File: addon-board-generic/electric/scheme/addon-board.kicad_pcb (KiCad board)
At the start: 2 copper layers, 57 parts, among them K1 CONN_3, K2 CONN_3, K3 CONN_3, K4 CONN_3, K5 CONN_3, K6 CONN_3, P1 TST, P10 CONN_6, P11 CONN_10, P12 CONN_4, P13 CONN_4, P2 TST, P3 cross board conn, P4 cross board conn, P5 TST, P6 TST, P7 TST, P8 TST, P9 CONN_4, Q1 NPN, Q2 MOS_P, Q3 BC847, Q4 BC847, Q5 MOS_P, Q6 MOS_P, U1 L293, U2 L293, U3 74HC165

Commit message: Added shift registers to increase IO pins number.
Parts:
- added K7, K8: CONN_3, PIN_ARRAY_3X1, F.Cu at (0.00, 0.00)
- added P10: CONN_8, PIN_ARRAY-8X1, F.Cu at (0.00, 0.00)
- added U4: 74HC595_MY, SO16E, F.Cu at (184.0, 157.5)
- added U5: 74HC595_MY, SO16E, F.Cu at (196.0, 157.5)
- P1, P2, P8: footprint PIN_ARRAY_1 -> m3-screw-hole
- P10: footprint PIN_ARRAY-6X1 -> PIN_ARRAY-8X1
- moved P9 285.0 mm to (185.5, 175.0)
- moved U2 276.7 mm to (212.5, 142.0)
- moved U1 259.0 mm to (194.5, 142.0)
- moved stm1 257.6 mm to (164.5, 156.5)
- moved P8 256.6 mm to (212.9, 157.0)
- moved U3 249.8 mm to (170.0, 169.5), turned to 180 degrees
- moved P2 220.6 mm to (148.0, 176.0)
- moved P3 214.8 mm to (145.5, 158.5), turned to 90 degrees
- moved P4 214.7 mm to (148.1, 158.5), turned to 90 degrees
- moved P1 190.0 mm to (148.1, 136.4)
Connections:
- P10 pad 6: GND -> /adc6
- P12 pad 1: /out4 -> /out3
- P12 pad 2: /out3 -> /out4
- P13 pad 1: /out8 -> /out7
- P13 pad 2: /out7 -> /out8
- U1 pad 13: /out4 -> /out3
- U1 pad 18: /out3 -> /out4
- U2 pad 13: /out8 -> /out7
- U2 pad 18: /out7 -> /out8
- stm1 pad 10: /adc4 -> /servo8
- stm1 pad 11: /adc5 -> /adc1
- stm1 pad 12: /servo6 -> /adc2
- stm1 pad 13: /wakeup -> /adc3
- stm1 pad 14: /servo-en -> /adc4
- stm1 pad 15: /adc1 -> /adc5
- stm1 pad 16: /adc2 -> /adc6
- stm1 pad 17: /adc3 -> /adc7
- stm1 pad 18: /addr0 -> /servo7
- stm1 pad 19: /addr1 -> /servo6
- stm1 pad 2: /moto8 -> (no net)
- stm1 pad 27: /led1 -> /addr0
- stm1 pad 28: /led2 -> /addr1
- stm1 pad 29: /moto-en1 -> /mr
- stm1 pad 3: /moto4 -> (no net)
- stm1 pad 30: /moto-en2 -> /oe
- stm1 pad 31: /moto5 -> /shcp
- stm1 pad 32: /moto6 -> /stcp
- stm1 pad 33: /moto7 -> /ds
- stm1 pad 4: /moto3 -> (no net)
- stm1 pad 5: /moto1 -> /wakeup
- stm1 pad 6: /moto2 -> (no net)
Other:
- board outline added: 85 x 56 mm
- net class Default: clearance 0.254 -> 0.2; trace_width 0.254 -> 0.25; via_dia 0.889 -> 0.9; via_drill 0.635 -> 0.6
- net class Power added: clearance 0.2, trace_width 0.5, via_dia 1, via_drill 0.7
- rule trace_clearance: 0.254 -> 0.2
- rule trace_min: 0.254 -> 0.1524
- rule via_min_drill: 0.508 -> 0.5
- rule via_min_size: 0.889 -> 0.8

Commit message: Placing components.
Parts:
- removed the P10 at (0.00, 0.00)
- moved P11 262.7 mm to (203.5, 178.2)
- moved Q6 258.0 mm to (208.8, 129.5), turned to 90 degrees
- moved R15 251.7 mm to (201.2, 134.5), turned to 180 degrees
- moved Q4 251.5 mm to (201.2, 131.8), turned to 180 degrees
- moved R17 248.9 mm to (206.8, 132.2), turned to 180 degrees
- moved R13 248.1 mm to (204.0, 133.8), turned to 270 degrees
- moved R7 245.8 mm to (184.2, 170.5), turned to 270 degrees
- moved R19 245.7 mm to (205.8, 129.5), turned to 90 degrees
- moved R8 245.6 mm to (179.2, 170.5), turned to 270 degrees
- moved R5 233.5 mm to (174.2, 162.5), turned to 270 degrees
- moved P10 232.4 mm to (163.8, 178.2)
- moved C5 232.0 mm to (178.5, 157.0), turned to 180 degrees
- moved D2 231.4 mm to (175.0, 127.2)
- moved C2 226.3 mm to (164.2, 154.0)
- moved C4 224.6 mm to (178.2, 147.2), turned to 270 degrees
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
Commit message: Placing components.
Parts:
- moved Q5 243.1 mm to (221.5, 74.5), turned to 90 degrees
- moved R16 235.9 mm to (219.5, 77.2), turned to 180 degrees
- moved Q3 235.6 mm to (215.5, 76.5), turned to 90 degrees
- moved R18 233.6 mm to (218.5, 74.5), turned to 90 degrees
- moved R14 230.7 mm to (213.8, 73.8)
- moved R12 229.9 mm to (212.8, 76.5), turned to 90 degrees
- moved R3 225.6 mm to (151.5, 170.0)
- moved C7 217.7 mm to (194.0, 74.8)
- moved Q2 217.1 mm to (194.0, 77.5), turned to 90 degrees
- moved R11 214.8 mm to (190.2, 78.2), turned to 180 degrees
- moved R10 210.6 mm to (187.2, 75.5), turned to 90 degrees
- moved R9 210.5 mm to (185.2, 75.5), turned to 90 degrees
- moved Q1 210.5 mm to (190.2, 75.5), turned to 90 degrees
- moved R15 75.7 mm to (214.5, 60.0), turned to 0 degrees
- moved U2 71.9 mm to (230.2, 63.5)
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
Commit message: Started routing.
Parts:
- added C10: 18p, SM0805, F.Cu at (152.9, 165.4)
- added C8: 10u, SM0805, F.Cu at (184.5, 135.6)
- added C9: 18p, SM0805, F.Cu at (152.9, 161.5)
- added R20: 50, SM0805, F.Cu at (159.0, 164.3)
- added X1: 8MHz, C2, F.Cu at (155.7, 163.6)
- C7: value 10u -> 100n
- P10: value CONN_6 -> CONN_8
- moved R15 104.2 mm to (220.1, 164.1), turned to 90 degrees
- moved R13 102.8 mm to (222.9, 165.1), turned to 180 degrees
- moved Q4 99.8 mm to (222.9, 162.3), turned to 180 degrees
- moved R19 98.9 mm to (220.9, 159.6), turned to 180 degrees
- moved Q6 96.1 mm to (220.9, 156.8), turned to 180 degrees
- moved R17 95.4 mm to (223.6, 158.8), turned to 270 degrees
- moved R14 95.3 mm to (206.6, 168.8), turned to 90 degrees
- moved R12 93.3 mm to (209.3, 169.8), turned to 180 degrees
- moved Q3 90.7 mm to (209.3, 167.0), turned to 180 degrees
- moved R18 90.2 mm to (207.3, 164.0), turned to 180 degrees
- moved Q5 87.7 mm to (207.3, 161.0), turned to 180 degrees
- moved R16 86.3 mm to (210.1, 163.0), turned to 270 degrees
- moved U2 78.5 mm to (218.9, 141.2), turned to 90 degrees
- moved R9 70.8 mm to (179.8, 146.1), turned to 180 degrees
- moved U1 69.0 mm to (205.0, 141.2), turned to 90 degrees
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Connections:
- stm1 pad 3: (no net) -> /wakeup
- stm1 pad 5: /wakeup -> N-0000044
- stm1 pad 6: (no net) -> N-0000042
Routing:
- net VDD: track 0.00 -> 24.2 mm
- net GND: track 0.01 -> 20.4 mm
- net N-0000044: track 0.00 -> 13.0 mm
- net /swd-io: track 0.00 -> 11.3 mm
- net /swd-clk: track 0.00 -> 8.04 mm
- net /buck-out-5v: track 0.00 -> 7.70 mm
- net /batt+: track 0.00 -> 7.70 mm
- net N-0000043: track 0.00 -> 6.73 mm
- net /iwakeup: track 0.00 -> 5.19 mm
- net N-0000042: track 0.00 -> 4.09 mm
- net /sda-int: track 0.00 -> 2.58 mm
- net /scl-int: track 0.00 -> 2.58 mm

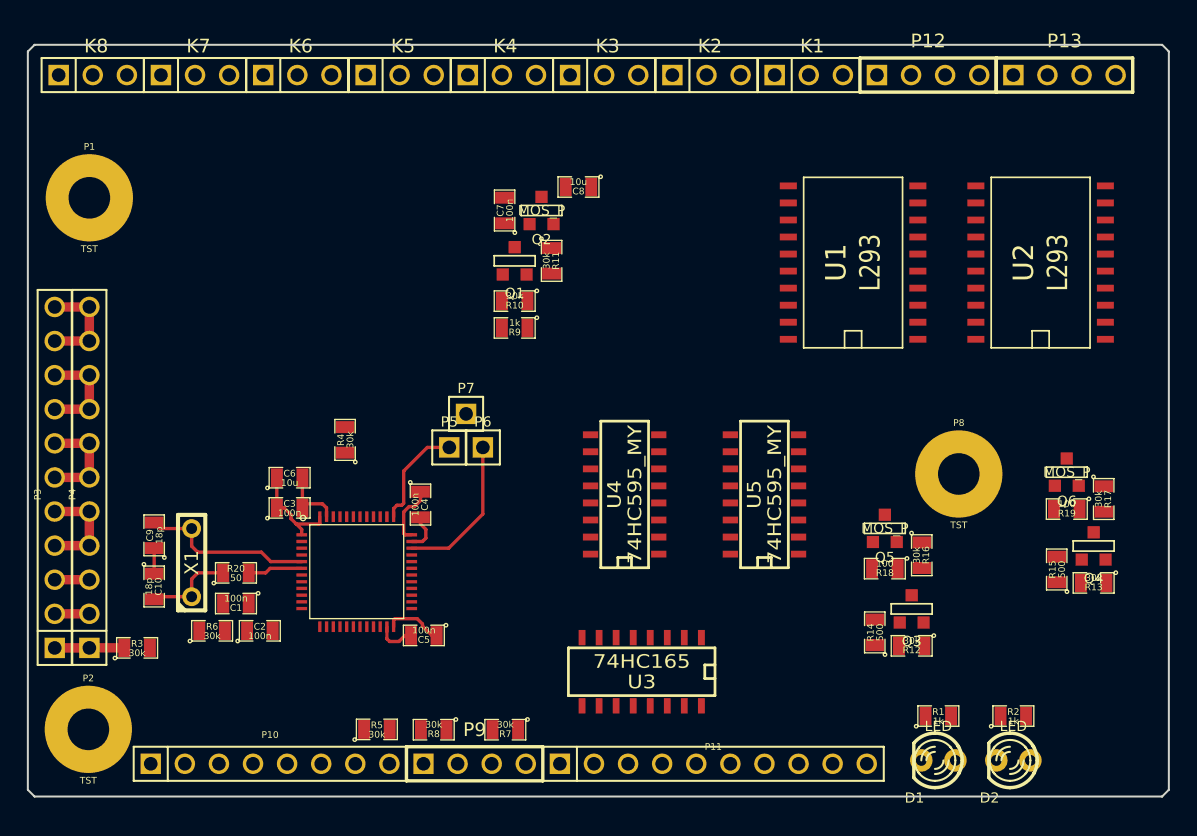
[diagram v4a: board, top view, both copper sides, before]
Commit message: Finished routing. Holes for supports and cross board socket matches should be checked!
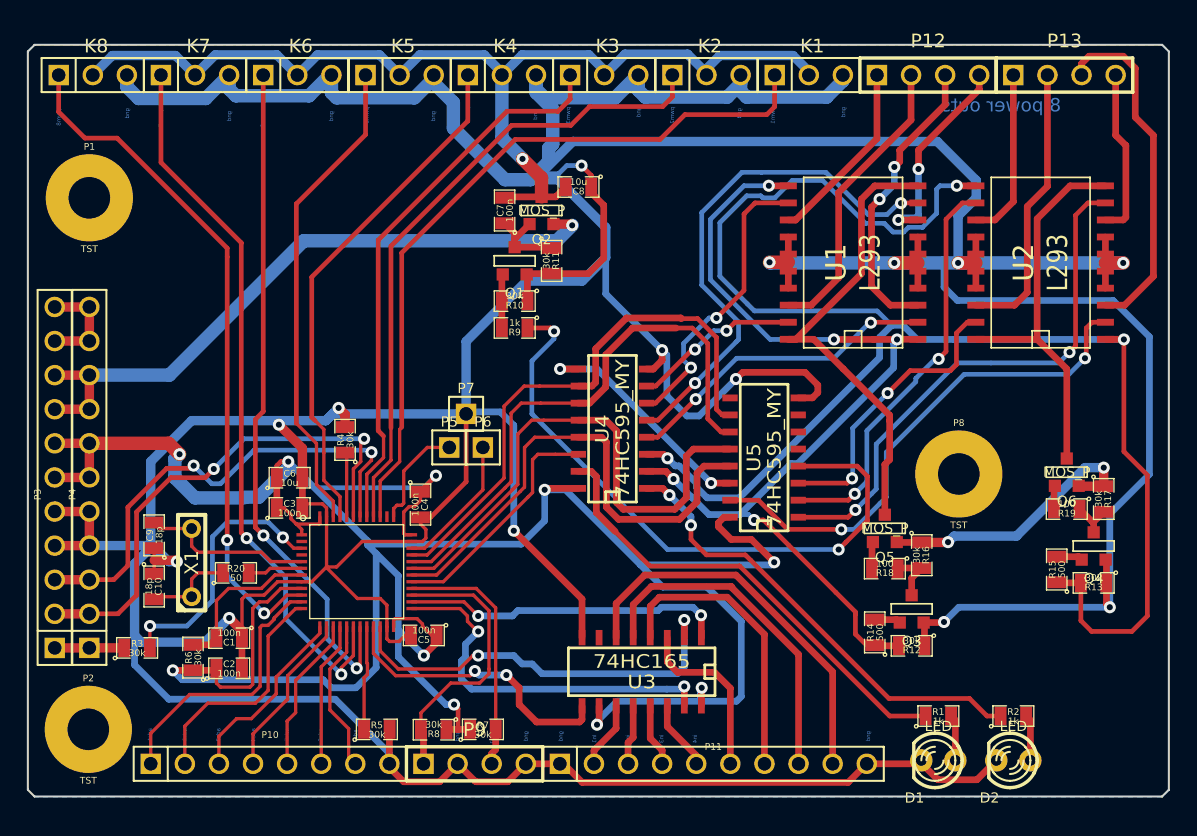
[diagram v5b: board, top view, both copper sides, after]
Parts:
- moved U4 4.98 mm to (187.1, 153.6)
- moved C2 3.61 mm to (158.5, 171.4)
- moved U5 2.75 mm to (198.3, 155.8)
- moved C1 2.62 mm to (158.5, 169.2)
- moved R6 2.45 mm to (155.8, 170.7), turned to 90 degrees
- moved R7 1.67 mm to (177.4, 176.0), turned to 0 degrees
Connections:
- stm1 pad 29: /mr -> /ds
- stm1 pad 31: /shcp -> /stcp
- stm1 pad 32: /stcp -> /shcp
- stm1 pad 33: /ds -> /mr
- stm1 pad 39: (no net) -> /servo1
- stm1 pad 40: (no net) -> /servo2
- stm1 pad 41: /servo1 -> /servo3
- stm1 pad 42: /servo2 -> /scl-int
- stm1 pad 43: /servo3 -> /sda-int
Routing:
- net GND: track 20.4 -> 538.0 mm, vias 0 -> 14
- net VDD: track 24.2 -> 208.9 mm, vias 0 -> 10
- net /moto-en2: track 0.00 -> 119.7 mm, vias 0 -> 3
- net /servo-vdd+: track 0.00 -> 78.0 mm, vias 0 -> 1
- net /moto-en1: track 0.00 -> 72.0 mm, vias 0 -> 5
- net /servo1: track 0.00 -> 55.0 mm
- net /servo7: track 0.00 -> 54.1 mm, vias 0 -> 2
- net /servo8: track 0.00 -> 51.2 mm, vias 0 -> 2
- net /servo6: track 0.00 -> 50.8 mm, vias 0 -> 2
- net /servo2: track 0.00 -> 47.9 mm
- net /servo-en: track 0.00 -> 47.8 mm, vias 0 -> 2
- net /batt+: track 7.70 -> 49.7 mm, vias 0 -> 1
- net /shcp: track 0.00 -> 41.8 mm
- net /mr: track 0.00 -> 41.8 mm
- net /servo3: track 0.00 -> 41.7 mm
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- added copper zone on B.Cu, net GND
- added copper zone on F.Cu, net GND
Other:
- board text added: "8 power outs"
- board text added: "adc1"
- board text added: "adc2"
- board text added: "adc3"
- board text added: "adc4"
- board text added: "adc5"
- board text added: "adc6"
- board text added: "adc7"
- board text added: "addr0"
- board text added: "addr1"
- board text added: "gnd"
- board text added: "in1"
- board text added: "in2"
- board text added: "in3"
- board text added: "in4"
- board text added: "in5"
- board text added: "in6"
- board text added: "in7"
- board text added: "in8"
- board text added: "pwm1"
- board text added: "pwm2"
- board text added: "pwm3"
- board text added: "pwm4"
- board text added: "pwm5"
- board text added: "pwm6"
- board text added: "pwm7"
- board text added: "pwm8"
